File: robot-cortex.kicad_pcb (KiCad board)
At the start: 4 copper layers, 27.5 x 26.9 mm, 79 parts, among them IC1 THVD2410VDRCR, J1 USB4110GFA, M1 THRU_HOLE_PAD, M2 THRU_HOLE_PAD, Q1 SS8050-G, Q2 SS8050-G, U1 C2901617, U10 TPS63070, U11 TPS63070, U2 STM32G431CBT6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

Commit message: updates to design - including new uart channels and rs485 channels
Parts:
- moved C36 22.0 mm to (178.9, 115.0), turned to -90 degrees
- moved IC1 20.4 mm to (181.4, 116.9)
- moved R19 20.0 mm to (179.0, 116.6)
- moved C1 19.1 mm to (183.7, 115.3), turned to -90 degrees
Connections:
- IC1 pad 8: /C- -> /RS1_B
- IC1 pad 9: /C+ -> /RS1_A
- R19 pad 1: /C- -> /RS1_B
- R19 pad 2: /C+ -> /RS1_A
- U3 pad 6: /C- -> /CANL
- U3 pad 7: /C+ -> /CANH
- U5 pad 2: /C- -> /CANL
- U5 pad 3: /C+ -> /CANH
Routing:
- net /UART1_TX: track 11.8 -> 0.00 mm, vias 2 -> 0
- net /C-: track 11.8 -> 0.00 mm
- net /C+: track 11.8 -> 0.00 mm
- net /UART1_RX: track 11.4 -> 0.00 mm
- net +3V3: track 59.8 -> 51.0 mm, vias 20 -> 18
- net /UART1_DE: track 6.42 -> 0.00 mm, vias 2 -> 0
- net /CANL: track 0.00 -> 3.60 mm
- net /CANH: track 0.00 -> 3.59 mm
- net /+5V0: track 47.5 -> 44.8 mm

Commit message: updates to pins, layout
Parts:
- added C28: 100nF, Capacitor_SMD:C_0402_1005Metric, F.Cu at (175.2, 100.0)
- added C31: 100nF, Capacitor_SMD:C_0402_1005Metric, F.Cu at (168.3, 110.1)
- added C37: 100nF, Capacitor_SMD:C_0402_1005Metric, F.Cu at (168.3, 99.2)
- added C38: 100nF, Capacitor_SMD:C_0402_1005Metric, F.Cu at (168.3, 101.2)
- added IC2: THVD2410VDRCR, robot-cortex:THVD2410VDRCR, F.Cu at (164.5, 111.5)
- added IC3: THVD2410VDRCR, robot-cortex:THVD2410VDRCR, F.Cu at (164.5, 100.5)
- added R18: 4.7k, robot-cortex:R_0402_1005Metric, F.Cu at (214.3, 115.0)
- added R20: 120, robot-cortex:R_0402_1005Metric, F.Cu at (169.7, 105.7)
- added R21: 120, robot-cortex:R_0402_1005Metric, F.Cu at (169.7, 94.8)
- added U12: DF52-4S-0.8H(21), robot-cortex:DF52-4S-0.8H(21), F.Cu at (177.2, 98.5)
- added U13: DF52-4S-0.8H(21), robot-cortex:DF52-4S-0.8H(21), F.Cu at (165.2, 105.9)
- added U14: DF52-4S-0.8H(21), robot-cortex:DF52-4S-0.8H(21), F.Cu at (165.2, 95.0)
- C1, C36, IC1, R19: moved to F.Cu
- moved R19 17.3 mm to (177.2, 99.4), turned to 180 degrees
- moved IC1 15.8 mm to (177.5, 101.6), turned to 90 degrees
- moved C1 15.4 mm to (175.2, 102.5)
- moved C36 11.0 mm to (168.3, 112.1), turned to 0 degrees
- moved D4 2.42 mm to (211.0, 115.9)
- moved R3 2.40 mm to (213.1, 115.9)
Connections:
- net /ENABLE renamed /I2S2_WS
- net /RS1_A renamed /RS485 Transceiver/RS1_B
- net /RS1_B renamed /RS485 Transceiver/RS1_A
- U2 pad 16: /ISENSE_A -> unconnected-(U2-PB0-Pad16)
- U2 pad 17: /ISENSE_B -> /LED
- U2 pad 22: /LED -> /UART3_TX
- U2 pad 25: /ISENSE_C -> /UART3_RX
- U2 pad 27: unconnected-(U2-PB13-Pad27) -> /I2S2_CK
- U2 pad 28: unconnected-(U2-PB14-Pad28) -> /USART3_DE
- U2 pad 29: unconnected-(U2-PB15-Pad29) -> /I2S2_SD
- U2 pad 31: unconnected-(U2-PA9-Pad31) -> /UART1_TX
- U2 pad 32: unconnected-(U2-PA10-Pad32) -> /UART1_RX
- U2 pad 39: unconnected-(U2-PA15-Pad39) -> /SS
- U2 pad 43: /UART1_TX -> unconnected-(U2-PB6-Pad43)
- U2 pad 44: /UART1_RX -> unconnected-(U2-PB7-Pad44)
- U2 pad 46: /SS -> unconnected-(U2-PB9-Pad46)
- U2 pad 8: /COS -> unconnected-(U2-PA0-Pad8)
- U2 pad 9: /SIN -> /USART2_DE
- U8 pad 29: /ESP32/ESP32_SS -> /SS
- U8 pad 30: /ESP32/ESP32_SCK -> /SPI1_MOSI
- U8 pad 31: /ESP32/ESP32_MISO -> /SPI1_MISO
- U8 pad 37: /ESP32/ESP32_MOSI -> /SPI1_SCK
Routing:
- net /RS485 Transceiver/RS1_A: track 0.00 -> 1.79 mm
- net /RS485 Transceiver/RS1_B: track 0.00 -> 1.79 mm
- net /BOOT: track 8.41 -> 9.91 mm
- net /+5V0: track 44.8 -> 46.2 mm
- net +3V3: track 51.0 -> 52.3 mm
- net /UART1_DE: track 0.00 -> 0.50 mm
- net GND: vias 57 -> 62
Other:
- board text added: "V3 R1"
- board text removed: "V2 R1"

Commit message: fix vbat
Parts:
- moved U13 24.1 mm to (175.9, 127.5), turned to -90 degrees
- moved R20 22.9 mm to (176.8, 127.5), turned to -90 degrees
- moved C28 22.9 mm to (176.9, 122.8), turned to 0 degrees
- moved C31 22.6 mm to (179.9, 129.6)
- moved U12 22.3 mm to (175.5, 120.8), turned to -90 degrees
- moved IC2 21.4 mm to (179.0, 127.2), turned to 180 degrees
- moved R19 21.4 mm to (176.4, 120.8), turned to -90 degrees
- moved C1 20.7 mm to (179.5, 122.8), turned to 0 degrees
- moved U14 20.0 mm to (173.8, 113.0), turned to -90 degrees
- moved C36 19.7 mm to (177.4, 129.6)
- moved R21 18.9 mm to (174.8, 113.0), turned to -90 degrees
- moved IC1 18.9 mm to (178.6, 120.5), turned to 180 degrees
- moved C37 18.5 mm to (177.9, 115.0)
- moved IC3 17.4 mm to (177.0, 112.8), turned to 180 degrees
- moved C38 15.6 mm to (175.3, 115.0)
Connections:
- U12 pad 1: /RS485 Transceiver/VBAT -> /VBAT
- U13 pad 1: /RS485 Transceiver1/VBAT -> /VBAT
- U14 pad 1: /RS485 Transceiver2/VBAT -> /VBAT
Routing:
- net /+5V0: track 46.2 -> 49.0 mm
- net +3V3: track 52.3 -> 54.9 mm
- net /RS485 Transceiver2/RS1_B: track 0.00 -> 1.79 mm
- net /RS485 Transceiver2/RS1_A: track 0.00 -> 1.79 mm
- net /RS485 Transceiver1/RS1_B: track 0.00 -> 1.79 mm
- net /RS485 Transceiver1/RS1_A: track 0.00 -> 1.79 mm
- net /USART3_DE: track 0.00 -> 0.50 mm
- net /USART2_DE: track 0.00 -> 0.50 mm

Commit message: routing
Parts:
- moved C36 39.3 mm to (215.8, 121.0), turned to 90 degrees
- moved U13 38.1 mm to (213.7, 122.5), turned to 0 degrees
- moved C31 37.5 mm to (215.8, 118.4), turned to 90 degrees
- moved R20 37.4 mm to (213.7, 121.6), turned to 0 degrees
- moved IC2 35.3 mm to (213.4, 119.3), turned to -90 degrees
- moved U14 31.5 mm to (203.9, 122.5), turned to 0 degrees
- moved C38 31.2 mm to (206.0, 121.0), turned to 90 degrees
- moved R21 30.4 mm to (203.9, 121.6), turned to 0 degrees
- moved C37 28.3 mm to (206.0, 118.4), turned to 90 degrees
- moved IC3 27.5 mm to (203.7, 119.3), turned to -90 degrees
- moved C28 19.6 mm to (196.5, 121.0), turned to 90 degrees
- moved U12 19.0 mm to (194.4, 122.5), turned to 0 degrees
- moved R19 18.1 mm to (194.4, 121.6), turned to 0 degrees
- moved C1 17.5 mm to (196.5, 118.4), turned to 90 degrees
- moved IC1 15.6 mm to (194.2, 119.3), turned to -90 degrees
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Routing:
- net /VBAT: track 23.5 -> 58.2 mm, vias 1 -> 3
- net /SS: track 0.00 -> 7.07 mm, vias 0 -> 1
- net /SPI1_MISO: track 0.00 -> 6.50 mm, vias 0 -> 1
- net /SPI1_MOSI: track 0.00 -> 5.31 mm, vias 0 -> 1
- net /ESP32/TCK: track 6.86 -> 11.9 mm, vias 1 -> 2
- net /SPI1_SCK: track 0.00 -> 5.00 mm, vias 0 -> 1
- net /UART2_RX: track 14.8 -> 18.3 mm, vias 1 -> 2
- net /ESP32/IO0: track 37.4 -> 40.1 mm
- net +3V3: track 54.9 -> 57.5 mm, vias 18 -> 21
- net /ESP32/TDI: track 10.1 -> 7.80 mm
- net /ESP32/TMS: track 12.8 -> 10.8 mm
- net /ESP32/TDO: track 15.2 -> 16.6 mm
- net /ESP32/EN: track 29.2 -> 30.5 mm
- net GND: vias 62 -> 67
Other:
- board size 27.5 x 26.9 mm -> 27.5 x 35.8 mm

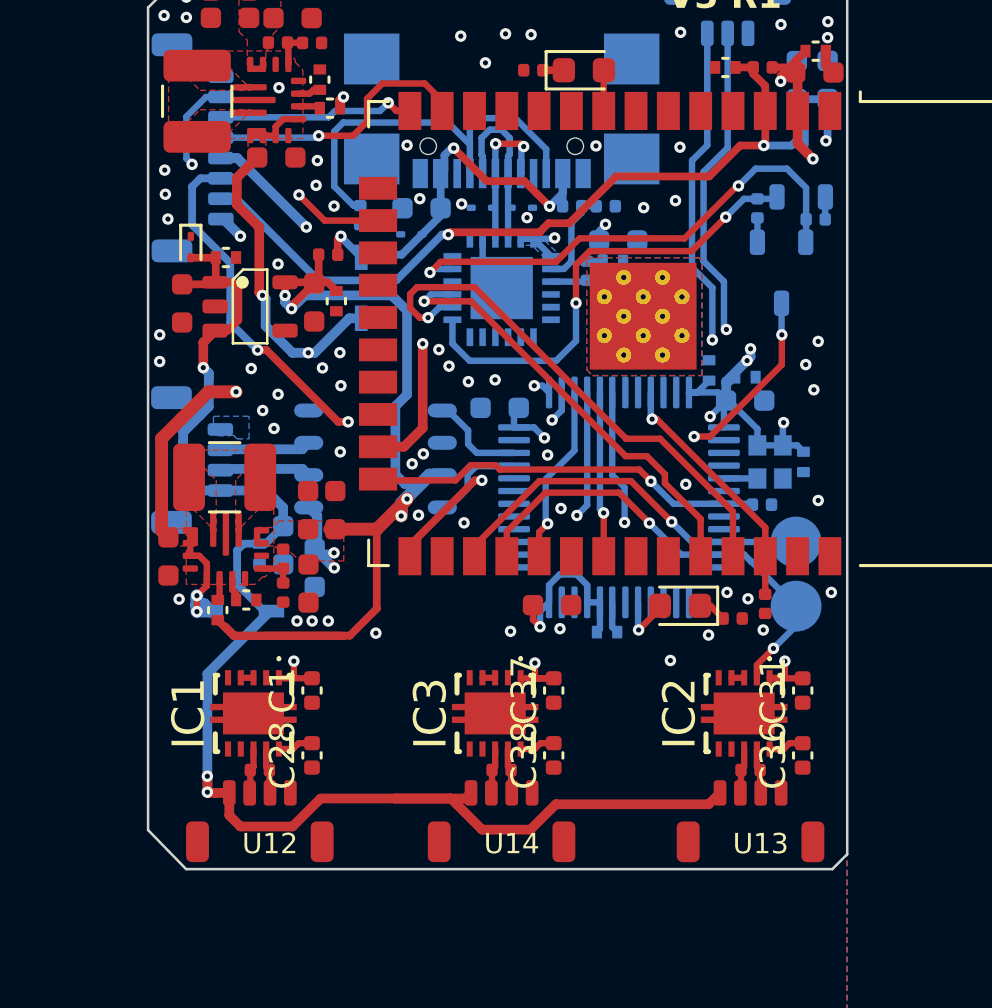
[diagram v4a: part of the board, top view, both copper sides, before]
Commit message: only spi pins remain
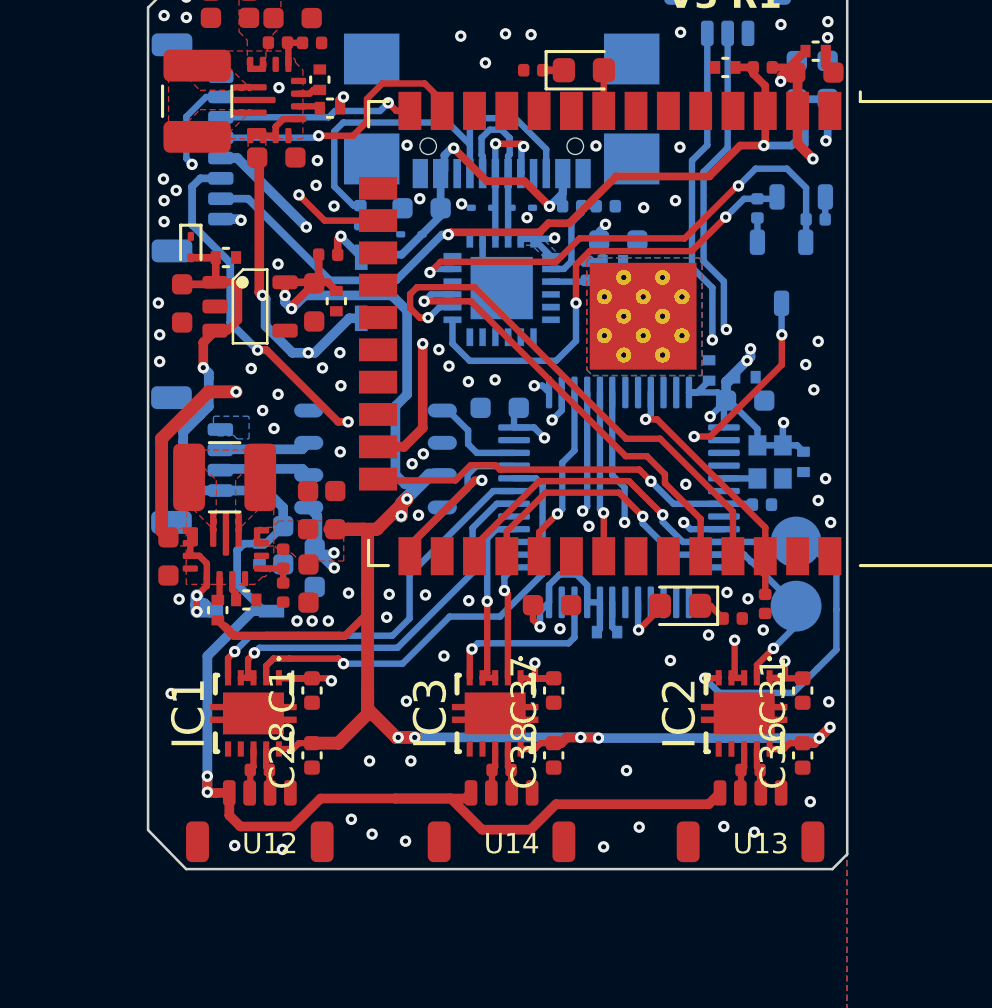
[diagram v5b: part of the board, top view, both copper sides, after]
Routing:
- net /+5V0: track 49.0 -> 80.5 mm, vias 4 -> 10
- net /UART1_RX: track 0.00 -> 17.7 mm, vias 0 -> 1
- net /UART1_TX: track 0.00 -> 15.7 mm, vias 0 -> 1
- net /UART1_DE: track 0.50 -> 15.2 mm, vias 0 -> 1
- net /UART2_TX: track 15.1 -> 27.1 mm, vias 1 -> 2
- net /USART2_DE: track 0.50 -> 9.18 mm, vias 0 -> 2
- net /UART3_TX: track 0.00 -> 6.76 mm, vias 0 -> 1
- net /USART3_DE: track 0.50 -> 7.26 mm, vias 0 -> 1
- net /UART3_RX: track 0.00 -> 4.55 mm, vias 0 -> 1
- net /VDD_MIXED: track 31.0 -> 30.3 mm
- net +3V3: track 57.5 -> 58.2 mm
- net GND: vias 67 -> 88

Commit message: routed, gotta check da pinz
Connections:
- U8 pad 30: /SPI1_MOSI -> /SPI1_SCK
- U8 pad 33: unconnected-(U8-IO21-Pad33) -> /SPI1_MOSI
- U8 pad 37: /SPI1_SCK -> unconnected-(U8-IO23-Pad37)
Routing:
- net /SPI1_MOSI: track 5.31 -> 7.88 mm
- net /SPI1_SCK: track 4.73 -> 6.69 mm

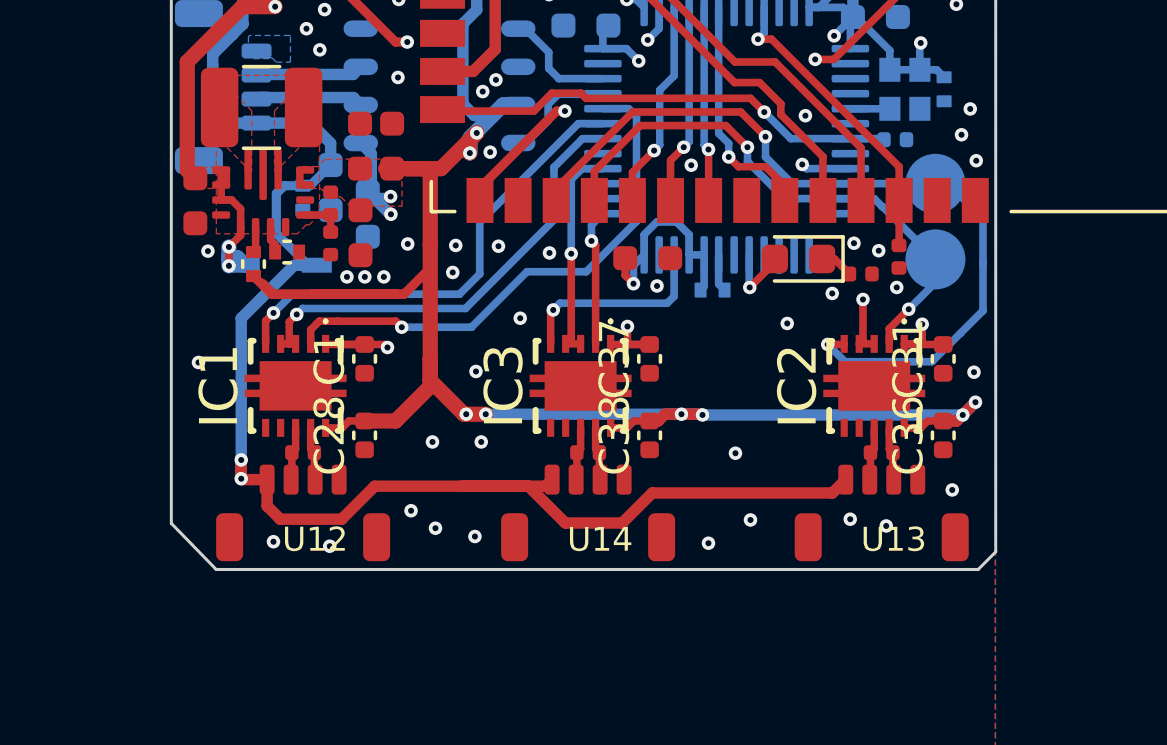
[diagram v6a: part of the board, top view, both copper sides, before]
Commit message: bom fix for fets, now refers to the part i am actually using not the one which doesn't work right. Library changes for parts missing courtyards, drc passing
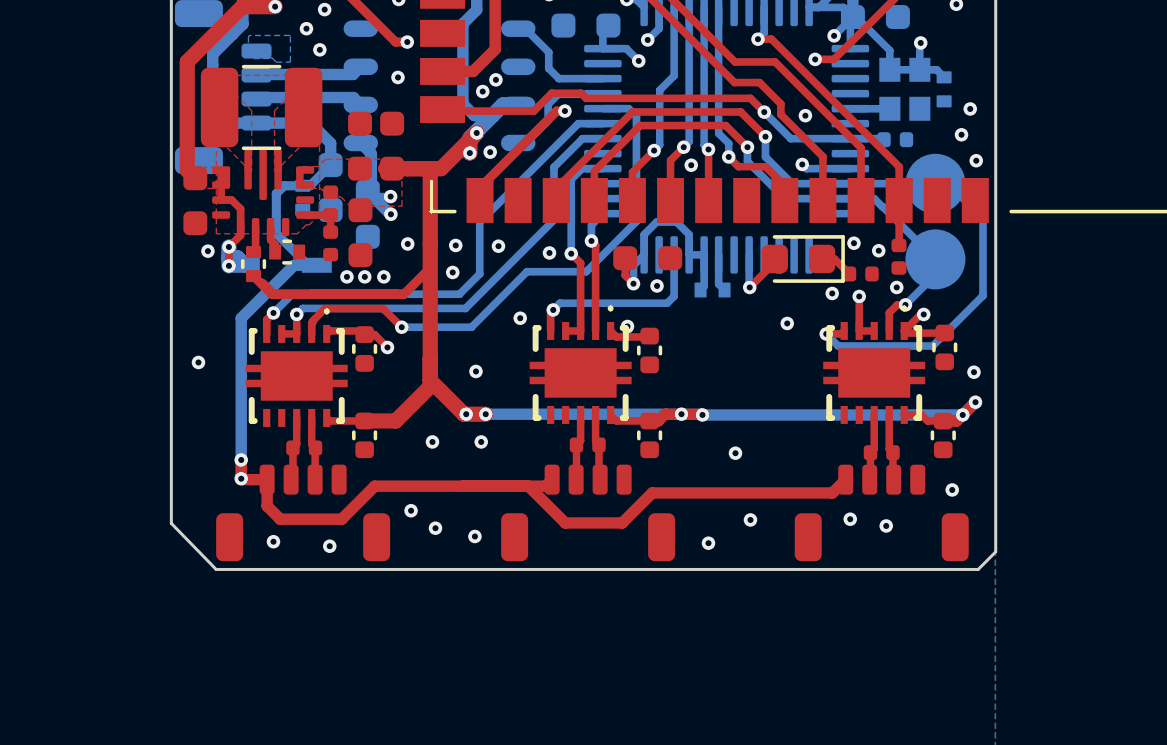
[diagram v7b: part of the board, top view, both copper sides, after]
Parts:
- Q1: value SS8050-G -> SSM3K15F,LF
- U4: value DF52-3S-0.8H(21) -> DF52-5S-0.8H(21)
- moved IC2 0.43 mm to (213.4, 118.9)
- moved IC3 0.43 mm to (203.7, 118.9)
- moved C31 0.38 mm to (215.8, 118.0)
- moved IC1 0.33 mm to (194.2, 119.0)
- moved C1 0.33 mm to (196.5, 118.1)
- moved C37 0.28 mm to (206.0, 118.2)
- moved R21 0.26 mm to (203.9, 121.3)
- moved R19 0.16 mm to (194.4, 121.4)
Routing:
- net +3V3: track 58.2 -> 56.4 mm
- net /USART2_DE: track 9.04 -> 8.50 mm

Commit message: bom updates
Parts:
- C22, C25: value C386081 -> 10uF
- C24, C27, C29, C30, C32, C33: value C2998534 -> 10uF
- U4: value DF52-5S-0.8H(21) -> DF52-3S-0.8H(21)
